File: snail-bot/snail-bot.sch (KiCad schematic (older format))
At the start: 31 parts

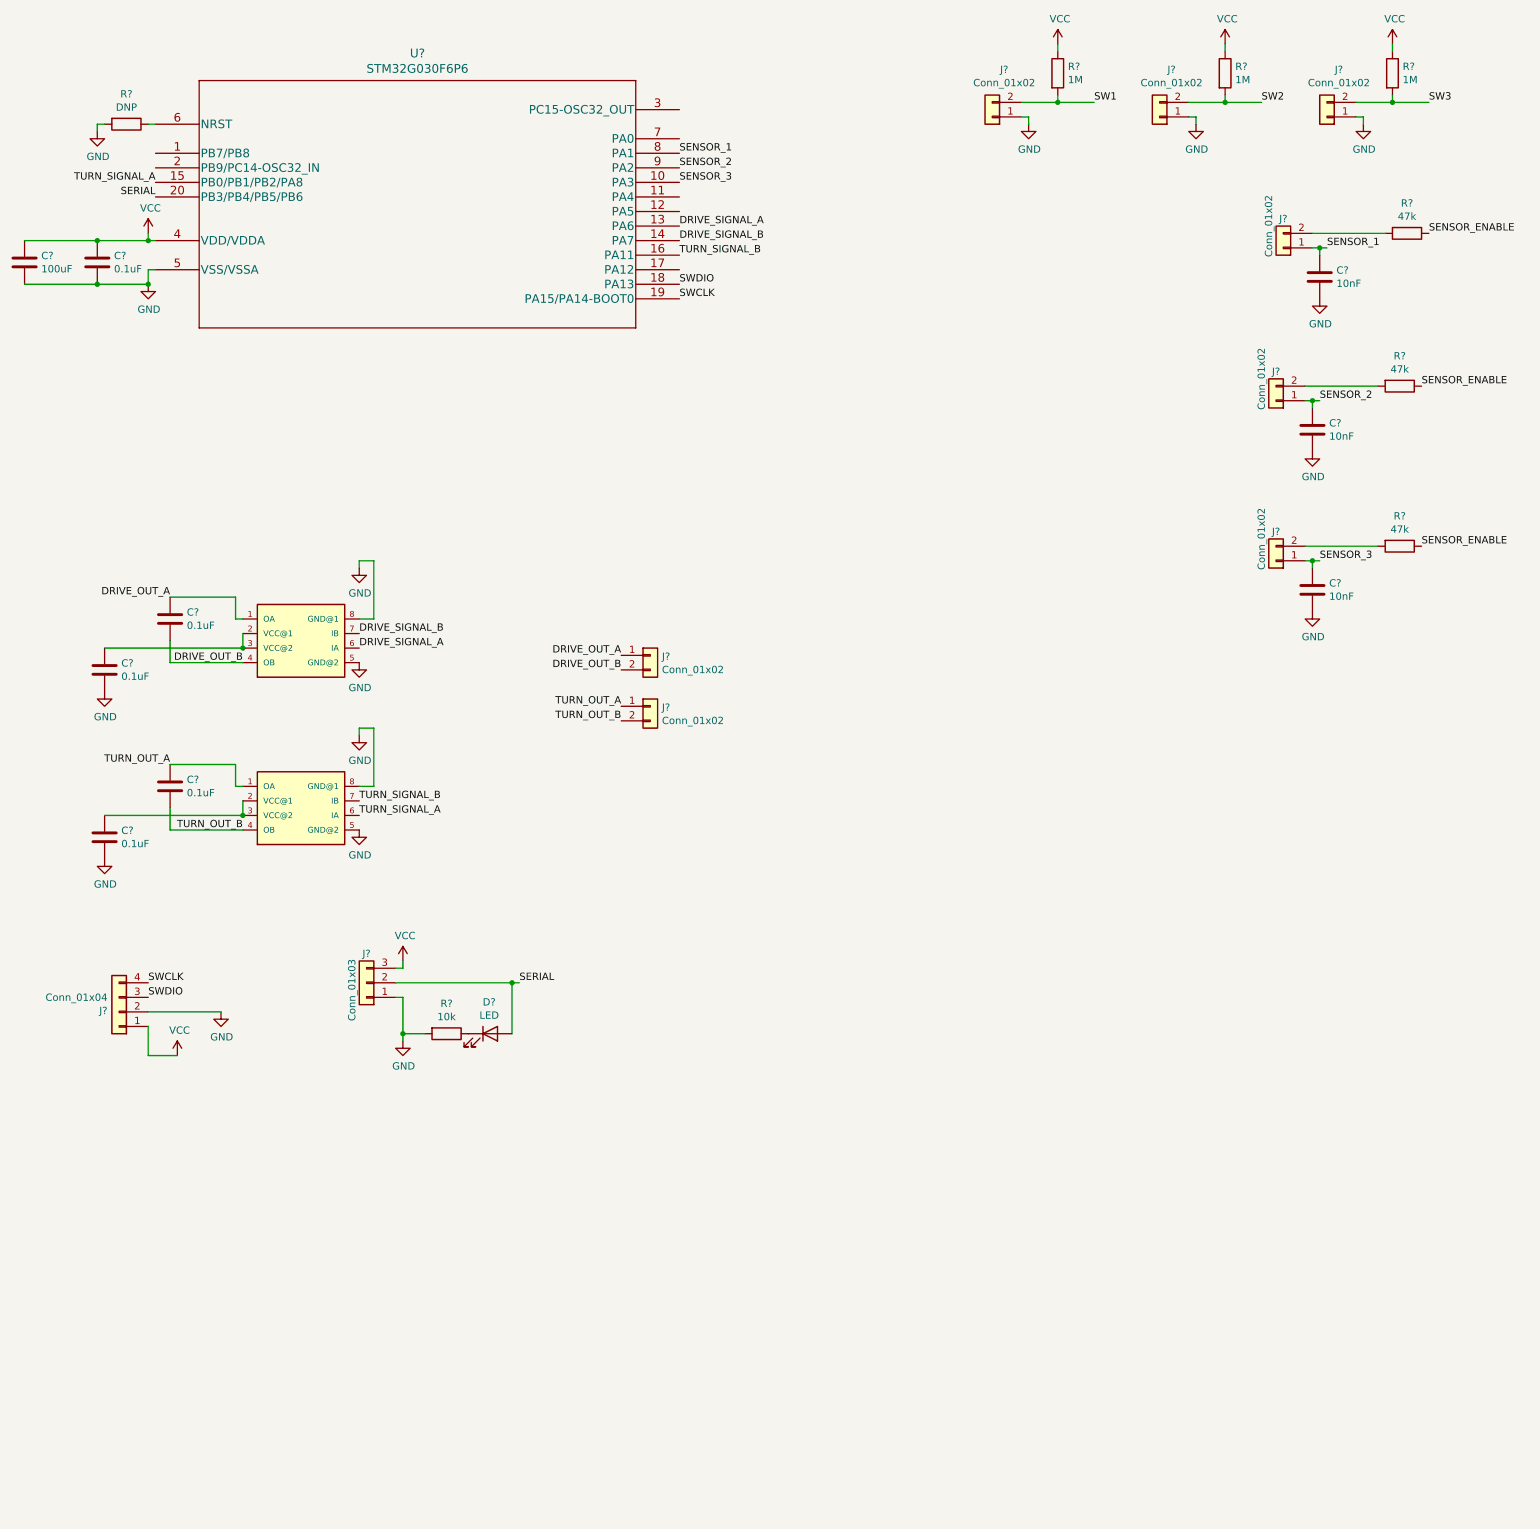
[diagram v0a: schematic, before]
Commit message: Schematic polish
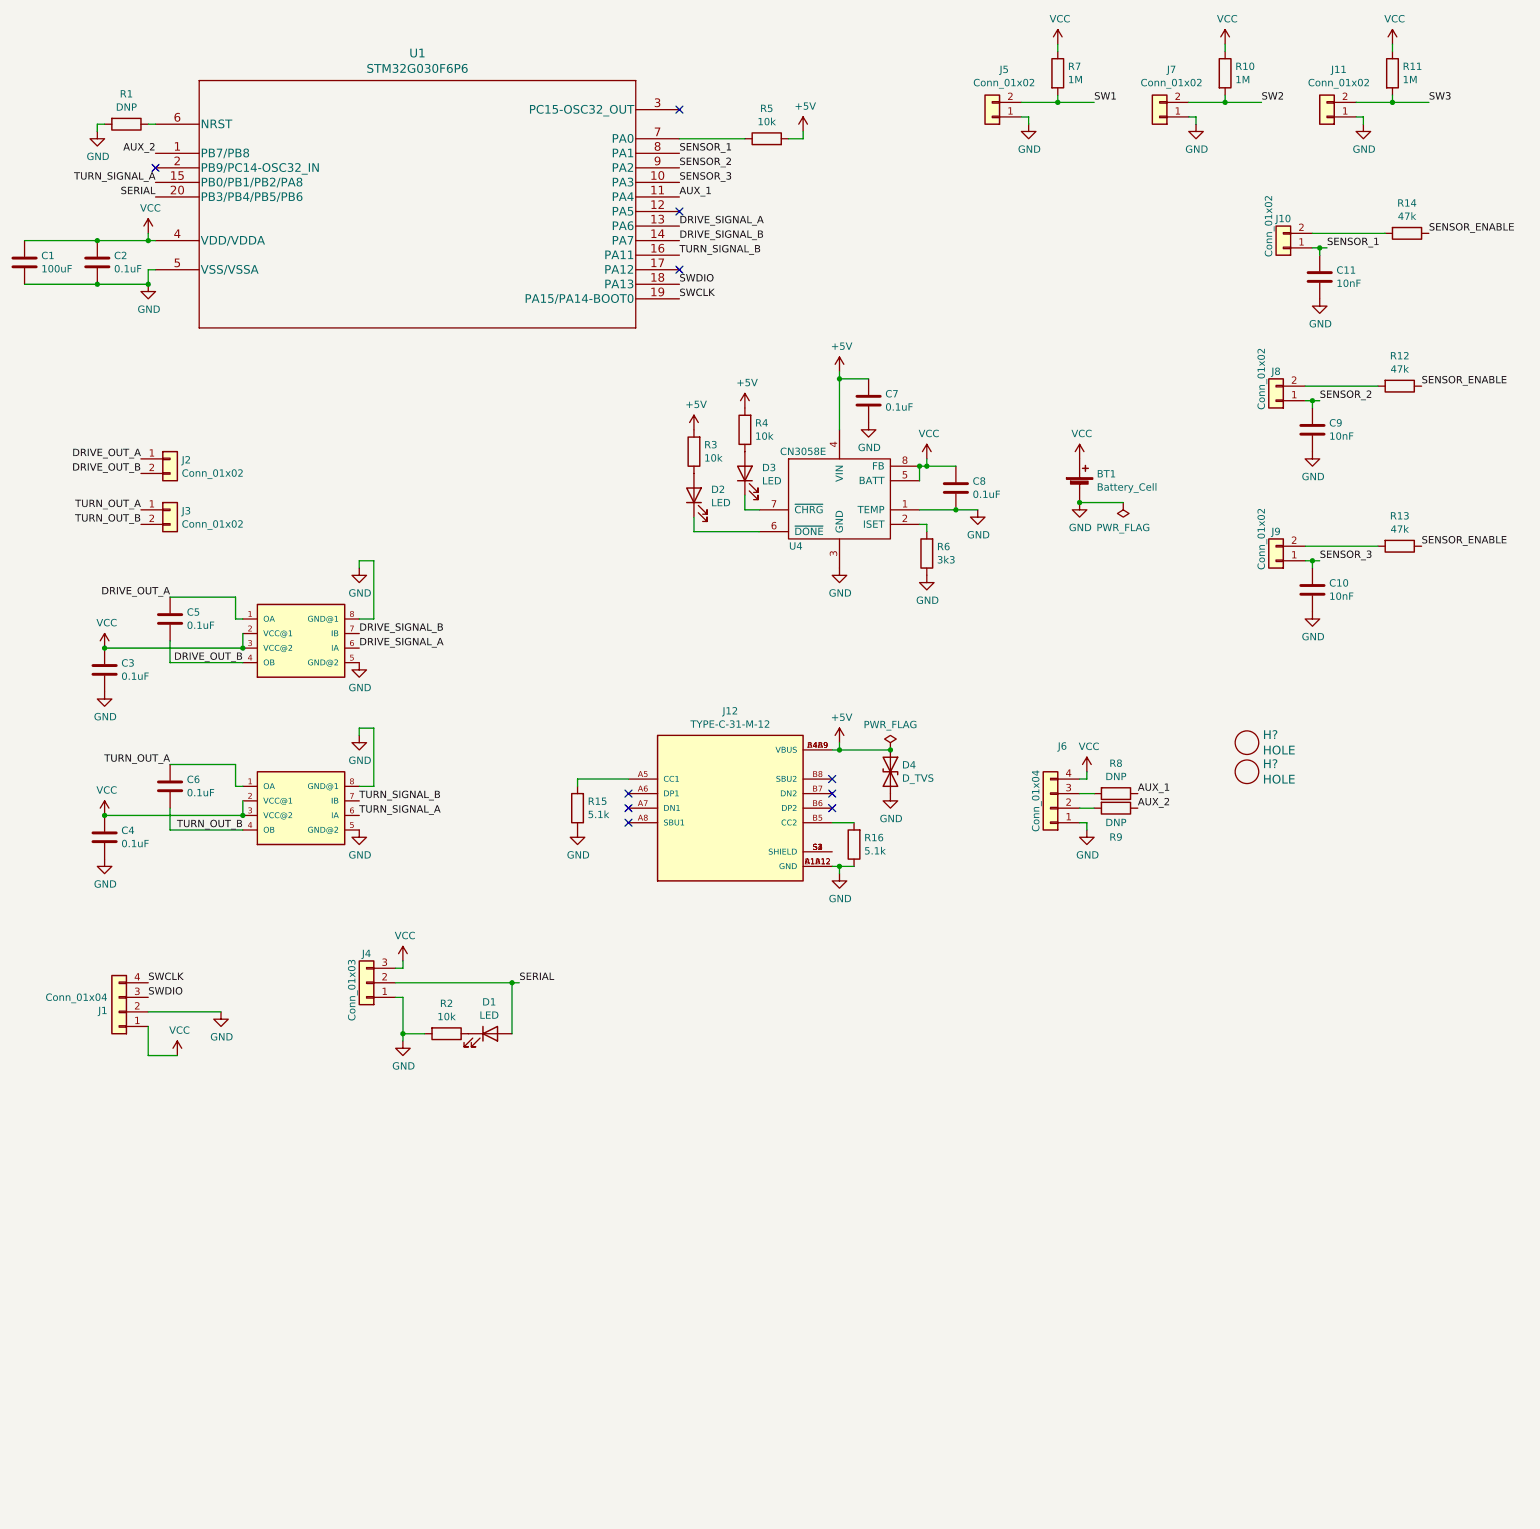
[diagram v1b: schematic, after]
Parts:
- added BT1: Battery_Cell, symbol Device:Battery_Cell
- added C7, C8: 0.1uF, Capacitor_SMD:C_0603_1608Metric, symbol Device:C
- added D2, D3: LED, LED_SMD:LED_0603_1608Metric, symbol Device:LED
- added D4: D_TVS, Diode_SMD:D_SMB, symbol Device:D_TVS
- added H? (x2): HOLE, symbol Homebrew:HOLE
- added J12: TYPE-C-31-M-12, snapeda:HRO_TYPE-C-31-M-12, symbol snapeda-TYPE-C-31-M-12:TYPE-C-31-M-12
- added J6: Conn_01x04, symbol Connector_Generic:Conn_01x04
- added R15, R16: 5.1k, Resistor_SMD:R_0603_1608Metric, symbol Device:R
- added R3, R4, R5: 10k, Resistor_SMD:R_0603_1608Metric, symbol Device:R
- added R6: 3k3, Resistor_SMD:R_0603_1608Metric, symbol Device:R
- added R8, R9: DNP, Resistor_SMD:R_0603_1608Metric, symbol Device:R
- added U4: CN3058E, homebrew:SOP-8_3.9x4.9mm_P1.27mm_Thermal, symbol Homebrew:CN3058E
- J5: renamed from J?; LCSC (none) -> C406141
- gave numbers to parts that had none: 30
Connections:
- net GND: now also BT1.2 (-), C7.2, C8.2, D4.2 (A2), J12.A1B12 (GND), J12.B1A12 (GND), J6.1 (Pin_1), R15.1, R16.1, R6.1, U4.1 (TEMP), U4.3 (GND)
- net VCC: now also C3.1, C4.1, U2.2 (VCC@1), U2.3 (VCC@2), U3.2 (VCC@1), U3.3 (VCC@2), BT1.1 (+), C8.1, J6.4 (Pin_4), U4.5 (BATT), U4.8 (FB)
- net AUX_2: now reaches U1.1 (PB7/PB8)
- net AUX_2: now also R9.1
- net AUX_1: now reaches U1.11 (PA4)
- net AUX_1: now also R8.1
- net at U1.7 (PA0): now also R5.1
- new net: R6.2, U4.2 (ISET)
- new net: D2.1 (K), U4.6 (~DONE)
- new net: D3.1 (K), U4.7 (~CHRG)
- new net: D3.2 (A), R4.1
- new net: D2.2 (A), R3.1
- new net: J6.2 (Pin_2), R9.2
- new net: J6.3 (Pin_3), R8.2
- new net: J12.A5 (CC1), R15.2
- new net: J12.B5 (CC2), R16.2
- new net: J12.S1 (SHIELD), J12.S2 (SHIELD), J12.S3 (SHIELD), J12.S4 (SHIELD)
- new net +5V: C7.1, D4.1 (A1), J12.A4B9 (VBUS), J12.B4A9 (VBUS), R3.2, R4.2, R5.2, U4.4 (VIN)
- no-connect marks 0 -> 10
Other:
- moved on the sheet: J2, J3

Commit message: Finish schematic and associations
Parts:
- removed J7, J8: Conn_01x02, symbol Connector_Generic:Conn_01x02
- added C4, C8: 0.1uF, Capacitor_SMD:C_0603_1608Metric, symbol Device:C
- added J1, J12, J13: Conn_01x02, homebrew:JST_ZH_XKB_SMD_1x02_P1.5mm_Horizontal, symbol Connector_Generic:Conn_01x02
- added U4: L9110, snapeda:SO-08, symbol snail-bot-rescue:L9110-snapeda-L9110
- BT1: footprint (none) -> Battery:BatteryHolder_Keystone_2460_1xAA
- H1, H2: renamed from H?; footprint (none) -> MountingHole:MountingHole_3.2mm_M3; symbol Homebrew:HOLE -> snail-bot-rescue:HOLE-Homebrew
- J10, J11, J2, J3, J9: footprint (none) -> homebrew:JST_ZH_XKB_SMD_1x02_P1.5mm_Horizontal; LCSC (none) -> C406141
- J4: renamed from J12; symbol snapeda-TYPE-C-31-M-12:TYPE-C-31-M-12 -> snail-bot-rescue:TYPE-C-31-M-12-snapeda-TYPE-C-31-M-12
- J5: renamed from J6; footprint (none) -> Connector_PinHeader_2.54mm:PinHeader_1x04_P2.54mm_Vertical
- J6: renamed from J1; footprint (none) -> Connector_PinHeader_2.54mm:PinHeader_1x04_P2.54mm_Vertical
- J7: renamed from J5; footprint (none) -> homebrew:JST_ZH_XKB_SMD_1x02_P1.5mm_Horizontal
- J8: renamed from J4; footprint (none) -> Connector_PinHeader_2.54mm:PinHeader_1x03_P2.54mm_Vertical
- U1: footprint TSSOP20 -> Package_SO:TSSOP-20_4.4x6.5mm_P0.65mm; symbol snapeda-STM32G030F6:STM32G030F6P6 -> snail-bot-rescue:STM32G030F6P6-snapeda-STM32G030F6; LCSC (none) -> C529330
- U2, U3: symbol snapeda-L9110:L9110 -> snail-bot-rescue:L9110-snapeda-L9110
- U5: renamed from U4; symbol Homebrew:CN3058E -> snail-bot-rescue:CN3058E-Homebrew
- renumbered C8 to C10, C9 to C11, C10 to C12, C11 to C13, C3 to C2, C4 to C3, C2 to C5, C5 to C6, C6 to C7, C7 to C9, D4 to D1, D1 to D4, R15 to R1, R7 to R10, R2 to R11, R10 to R12, R12 to R13, R13 to R14, R14 to R15, R11 to R16, R1 to R2, R16 to R3, R3 to R4, R4 to R5, R8 to R6, R9 to R7, R6 to R8, R5 to R9
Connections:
- net GND: now also J9.1 (Pin_1), C4.2, J13.1 (Pin_1), U4.5 (GND@2), U4.8 (GND@1); no longer J11.1 (Pin_1)
- net SENSOR_1: now also J12.1 (Pin_1); no longer J10.1 (Pin_1)
- net SENSOR_2: now also J10.1 (Pin_1)
- net SENSOR_3: now also J11.1 (Pin_1); no longer J9.1 (Pin_1)
- net SW2: now also J9.2 (Pin_2)
- net SW3: now also J13.2 (Pin_2); no longer J11.2 (Pin_2)
- net VCC: now also C4.1, U4.2 (VCC@1), U4.3 (VCC@2)
- net MOTOR_SIGNAL_1B: now reaches U1.12 (PA5)
- net MOTOR_SIGNAL_1B: now also U2.7 (IB)
- net MOTOR_SIGNAL_3B: now reaches U1.17 (PA12)
- net MOTOR_SIGNAL_3B: now also U4.7 (IB)
- net at R15.2: now also J12.2 (Pin_2); no longer J10.2 (Pin_2)
- net at R13.2: now also J10.2 (Pin_2)
- net at R14.2: now also J11.2 (Pin_2); no longer J9.2 (Pin_2)
- net DRIVE_OUT_A renamed MOTOR_OUT_1A
- net MOTOR_OUT_1A: now also J1.1 (Pin_1); no longer J2.1 (Pin_1)
- net DRIVE_OUT_B renamed MOTOR_OUT_1B
- net MOTOR_OUT_1B: now also J1.2 (Pin_2); no longer J2.2 (Pin_2)
- net DRIVE_SIGNAL_A renamed MOTOR_SIGNAL_1A
- net DRIVE_SIGNAL_B renamed MOTOR_SIGNAL_2A
- net MOTOR_SIGNAL_2A: now also U3.6 (IA); no longer U2.7 (IB)
- net TURN_OUT_A renamed MOTOR_OUT_2A
- net MOTOR_OUT_2A: now also J2.1 (Pin_1); no longer J3.1 (Pin_1)
- net TURN_OUT_B renamed MOTOR_OUT_2B
- net MOTOR_OUT_2B: now also J2.2 (Pin_2); no longer J3.2 (Pin_2)
- net TURN_SIGNAL_A renamed MOTOR_SIGNAL_2B
- net MOTOR_SIGNAL_2B: now also U3.7 (IB); no longer U3.6 (IA)
- net TURN_SIGNAL_B renamed MOTOR_SIGNAL_3A
- net MOTOR_SIGNAL_3A: now also U4.6 (IA); no longer U3.7 (IB)
- new net MOTOR_OUT_3A: C8.1, J3.1 (Pin_1), U4.1 (OA)
- new net MOTOR_OUT_3B: C8.2, J3.2 (Pin_2), U4.4 (OB)
- no-connect marks 10 -> 8
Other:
- note added: "Power"
- moved on the sheet: BT1, C10, C11, C12, C13, C2, C3, C6, C7, C9, D1, D2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

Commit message: snail-bot v1.0
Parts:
- removed J5: Conn_01x04, Connector_PinHeader_2.54mm:PinHeader_1x04_P2.54mm_Vertical, symbol Connector_Generic:Conn_01x04
- removed R4: 10k, Resistor_SMD:R_0603_1608Metric, symbol Device:R
- removed R6, R7: DNP, Resistor_SMD:R_0603_1608Metric, symbol Device:R
- D2: LCSC C2286 -> C72043
- R2: footprint Resistor_SMD:R_0603_1608Metric_Pad0.98x0.95mm_HandSolder -> Resistor_SMD:R_0603_1608Metric_Pad1.05x0.95mm_HandSolder
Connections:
- net AUX_1 is gone; now on net SW1: U1.11 (PA4)
- net AUX_2 is gone; now on net SW3: U1.1 (PB7/PB8)
- net MOTOR_OUT_1A: now also J1.2 (Pin_2); no longer J1.1 (Pin_1)
- net MOTOR_OUT_1B: now also J1.1 (Pin_1); no longer J1.2 (Pin_2)
- net MOTOR_OUT_2A: now also J2.2 (Pin_2); no longer J2.1 (Pin_1)
- net MOTOR_OUT_2B: now also J2.1 (Pin_1); no longer J2.2 (Pin_2)
- net MOTOR_OUT_3A: now also J3.2 (Pin_2); no longer J3.1 (Pin_1)
- net MOTOR_OUT_3B: now also J3.1 (Pin_1); no longer J3.2 (Pin_2)
- net SENSOR_ENABLE: now also U1.2 (PB9/PC14-OSC32_IN)
- net SW2: now also U1.3 (PC15-OSC32_OUT)
- net at D3.2 (A), R5.1: now also D2.2 (A)
- no-connect marks 8 -> 6
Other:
- moved on the sheet: R2
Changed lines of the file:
@@
 L Device:R R2
 U 1 1 6195582F
-P 1450 1250
-F 0 "R2" V 1243 1250 50  0000 C CNN
-F 1 "DNP" V 1334 1250 50  0000 C CNN
-F 2 "Resistor_SMD:R_0603_1608Metric_Pad0.98x0.95mm_HandSolder" V 1380 1250 50  0001 C CNN
-F 3 "~" H 1450 1250 50  0001 C CNN
-	1    1450 1250
-	0    1    1    0
+P 1600 1100
+F 0 "R2" V 1393 1100 50  0000 C CNN
+F 1 "DNP" V 1484 1100 50  0000 C CNN
+F 2 "Resistor_SMD:R_0603_1608Metric_Pad1.05x0.95mm_HandSolder" V 1530 1100 50  0001 C CNN
+F 3 "~" H 1600 1100 50  0001 C CNN
+	1    1600 1100
+	-1   0    0    1
 $EndComp
 $Comp
 L power:GND #PWR08
 U 1 1 61955BB3
-P 1250 1300
-F 0 "#PWR08" H 1250 1050 50  0001 C CNN
-F 1 "GND" H 1255 1127 50  0000 C CNN
-F 2 "" H 1250 1300 50  0001 C CNN
-F 3 "" H 1250 1300 50  0001 C CNN
-	1    1250 1300
-	1    0    0    -1
-$EndComp
-Wire Wire Line
-	1250 1300 1250 1250
-Wire Wire Line
-	1250 1250 1300 1250
+P 1400 950
+F 0 "#PWR08" H 1400 700 50  0001 C CNN
+F 1 "GND" H 1405 777 50  0000 C CNN
+F 2 "" H 1400 950 50  0001 C CNN
+F 3 "" H 1400 950 50  0001 C CNN
+	1    1400 950
+	1    0    0    -1
+$EndComp
 Wire Wire Line
 	1650 1250 1600 1250
@@
 	750  2350 1250 2350
 Connection ~ 1250 2350
+Text Label 1550 3650 2    50   ~ 0
+MOTOR_OUT_1A
 Text Label 1550 3550 2    50   ~ 0
-MOTOR_OUT_1A
-Text Label 1550 3650 2    50   ~ 0
 MOTOR_OUT_1B
 $Comp
@@
 F 2 "LED_SMD:LED_0603_1608Metric" H 3850 10050 50  0001 C CNN
 F 3 "~" H 3850 10050 50  0001 C CNN
-F 4 "C2286" H 3850 10050 50  0001 C CNN "LCSC"
+F 4 "C72043" H 3850 10050 50  0001 C CNN "LCSC"
 	1    3850 10050
 	0    -1   -1   0
@@
 $EndComp
 $Comp
-L Device:R R4
-U 1 1 61A5AF44
-P 3850 9750
-F 0 "R4" H 3780 9704 50  0000 R CNN
-F 1 "10k" H 3780 9795 50  0000 R CNN
-F 2 "Resistor_SMD:R_0603_1608Metric" V 3780 9750 50  0001 C CNN
-F 3 "~" H 3850 9750 50  0001 C CNN
-F 4 "C25804" H 3850 9750 50  0001 C CNN "LCSC"
-	1    3850 9750
-	-1   0    0    1
-$EndComp
-$Comp
 L power:+5V #PWR021
 U 1 1 61A5B776
@@
 F 3 "" H 4200 9450 50  0001 C CNN
 	1    4200 9450
-	1    0    0    -1
-$EndComp
-$Comp
-L power:+5V #PWR020
-U 1 1 61A5BEC9
-P 3850 9600
-F 0 "#PWR020" H 3850 9450 50  0001 C CNN
-F 1 "+5V" H 3865 9773 50  0000 C CNN
-F 2 "" H 3850 9600 50  0001 C CNN
-F 3 "" H 3850 9600 50  0001 C CNN
-	1    3850 9600
 	1    0    0    -1
 $EndComp
@@
 F 3 "" H 6500 10100 50  0001 C CNN
 	1    6500 10100
-	1    0    0    -1
-$EndComp
-Text Label 5250 1750 0    50   ~ 0
-AUX_1
-Text Label 1650 1450 2    50   ~ 0
-AUX_2
-$Comp
-L Connector_Generic:Conn_01x04 J5
-U 1 1 61A7B959
-P 4750 4300
-F 0 "J5" H 4668 3875 50  0000 C CNN
-F 1 "Conn_01x04" V 4850 4250 50  0000 C CNN
-F 2 "Connector_PinHeader_2.54mm:PinHeader_1x04_P2.54mm_Vertical" H 4750 4300 50  0001 C CNN
-F 3 "~" H 4750 4300 50  0001 C CNN
-	1    4750 4300
-	-1   0    0    1
-$EndComp
-$Comp
-L power:VCC #PWR024
-U 1 1 61A7C0F1
-P 5000 4050
-F 0 "#PWR024" H 5000 3900 50  0001 C CNN
-F 1 "VCC" H 5015 4223 50  0000 C CNN
-F 2 "" H 5000 4050 50  0001 C CNN
-F 3 "" H 5000 4050 50  0001 C CNN
-	1    5000 4050
-	1    0    0    -1
-$EndComp
-$Comp
-L power:GND #PWR025
-U 1 1 61A7D90C
-P 5000 4450
-F 0 "#PWR025" H 5000 4200 50  0001 C CNN
-F 1 "GND" H 5005 4277 50  0000 C CNN
-F 2 "" H 5000 4450 50  0001 C CNN
-F 3 "" H 5000 4450 50  0001 C CNN
-	1    5000 4450
-	1    0    0    -1
-$EndComp
-Wire Wire Line
-	4950 4100 5000 4100
-Wire Wire Line
-	5000 4100 5000 4050
-Wire Wire Line
-	4950 4400 5000 4400
-Wire Wire Line
-	5000 4400 5000 4450
-$Comp
-L Device:R R6
-U 1 1 61A82CD6
-P 5200 4200
-F 0 "R6" V 4993 4200 50  0000 C CNN
-F 1 "DNP" V 5084 4200 50  0000 C CNN
-F 2 "Resistor_SMD:R_0603_1608Metric" V 5130 4200 50  0001 C CNN
-F 3 "~" H 5200 4200 50  0001 C CNN
-	1    5200 4200
-	0    1    1    0
-$EndComp
-$Comp
-L Device:R R7
-U 1 1 61A839B8
-P 5200 4300
-F 0 "R7" V 5400 4300 50  0000 C CNN
-F 1 "DNP" V 5300 4300 50  0000 C CNN
-F 2 "Resistor_SMD:R_0603_1608Metric" V 5130 4300 50  0001 C CNN
-F 3 "~" H 5200 4300 50  0001 C CNN
-	1    5200 4300
-	0    1    1    0
-$EndComp
-Text Label 5350 4200 0    50   ~ 0
-AUX_1
-Text Label 5350 4300 0    50   ~ 0
-AUX_2
-Wire Wire Line
-	5050 4200 4950 4200
-Wire Wire Line
-	4950 4300 5050 4300
-NoConn ~ 5250 1150
-NoConn ~ 1650 1550
-$Comp
-L snail-bot-rescue:STM32G030F6P6-snapeda-STM32G030F6 U1
-U 1 1 61952A14
-P 1650 1250
-F 0 "U1" H 3450 1737 60  0000 C CNN
-F 1 "STM32G030F6P6" H 3450 1631 60  0000 C CNN
-F 2 "Package_SO:TSSOP-20_4.4x6.5mm_P0.65mm" H 3450 1590 60  0001 C CNN
-F 3 "" H 1650 1250 60  0000 C CNN
-F 4 "C529330" H 1650 1250 50  0001 C CNN "LCSC"
-	1    1650 1250
 	1    0    0    -1
 $EndComp
@@
 $EndComp
 Text Label 1550 3900 2    50   ~ 0
-MOTOR_OUT_2A
-Text Label 1550 4000 2    50   ~ 0
 MOTOR_OUT_2B
+Text Label 1550 4350 2    50   ~ 0
+MOTOR_OUT_3A
 Text Label 1550 4250 2    50   ~ 0
-MOTOR_OUT_3A
-Text Label 1550 4350 2    50   ~ 0
 MOTOR_OUT_3B
 Connection ~ 900  7550
@@
 	1    0    0    -1
 $EndComp
+Text Label 1550 4000 2    50   ~ 0
+MOTOR_OUT_2A
+$Comp
+L snail-bot-rescue:STM32G030F6P6-snapeda-STM32G030F6 U1
+U 1 1 61952A14
+P 1650 1250
+F 0 "U1" H 3450 1737 60  0000 C CNN
+F 1 "STM32G030F6P6" H 3450 1631 60  0000 C CNN
+F 2 "Package_SO:TSSOP-20_4.4x6.5mm_P0.65mm" H 3450 1590 60  0001 C CNN
+F 3 "" H 1650 1250 60  0000 C CNN
+F 4 "C529330" H 1650 1250 50  0001 C CNN "LCSC"
+	1    1650 1250
+	1    0    0    -1
+$EndComp
+Wire Wire Line
+	4200 9750 3850 9750
+Wire Wire Line
+	3850 9750 3850 9900
+Connection ~ 4200 9750
+Text Label 1650 1550 2    50   ~ 0
+SENSOR_ENABLE
+Wire Wire Line
+	1600 950  1400 950
+Text Label 5250 1750 0    50   ~ 0
+SW1
+Text Label 5250 1150 0    50   ~ 0
+SW2
+Text Label 1650 1450 2    50   ~ 0
+SW3
 $EndSCHEMATC

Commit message: Add 3D models
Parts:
- J4: footprint snapeda:HRO_TYPE-C-31-M-12 -> homebrew:HRO_TYPE-C-31-M-12
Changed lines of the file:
@@
 F 0 "J4" H 1850 10517 50  0000 C CNN
 F 1 "TYPE-C-31-M-12" H 1850 10426 50  0000 C CNN
-F 2 "snapeda:HRO_TYPE-C-31-M-12" H 1850 9850 50  0001 L BNN
+F 2 "homebrew:HRO_TYPE-C-31-M-12" H 1850 9850 50  0001 L BNN
 F 3 "" H 1850 9850 50  0001 L BNN
 F 4 "HRO Electronics" H 1850 9850 50  0001 L BNN "MANUFACTURER"
